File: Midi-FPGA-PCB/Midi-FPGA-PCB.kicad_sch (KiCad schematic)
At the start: 20 parts, among them Q1 DMP2123L, SW1 Boot, SW2 Reset, U1 ESP32-WROOM-32, U2 AP7361EA

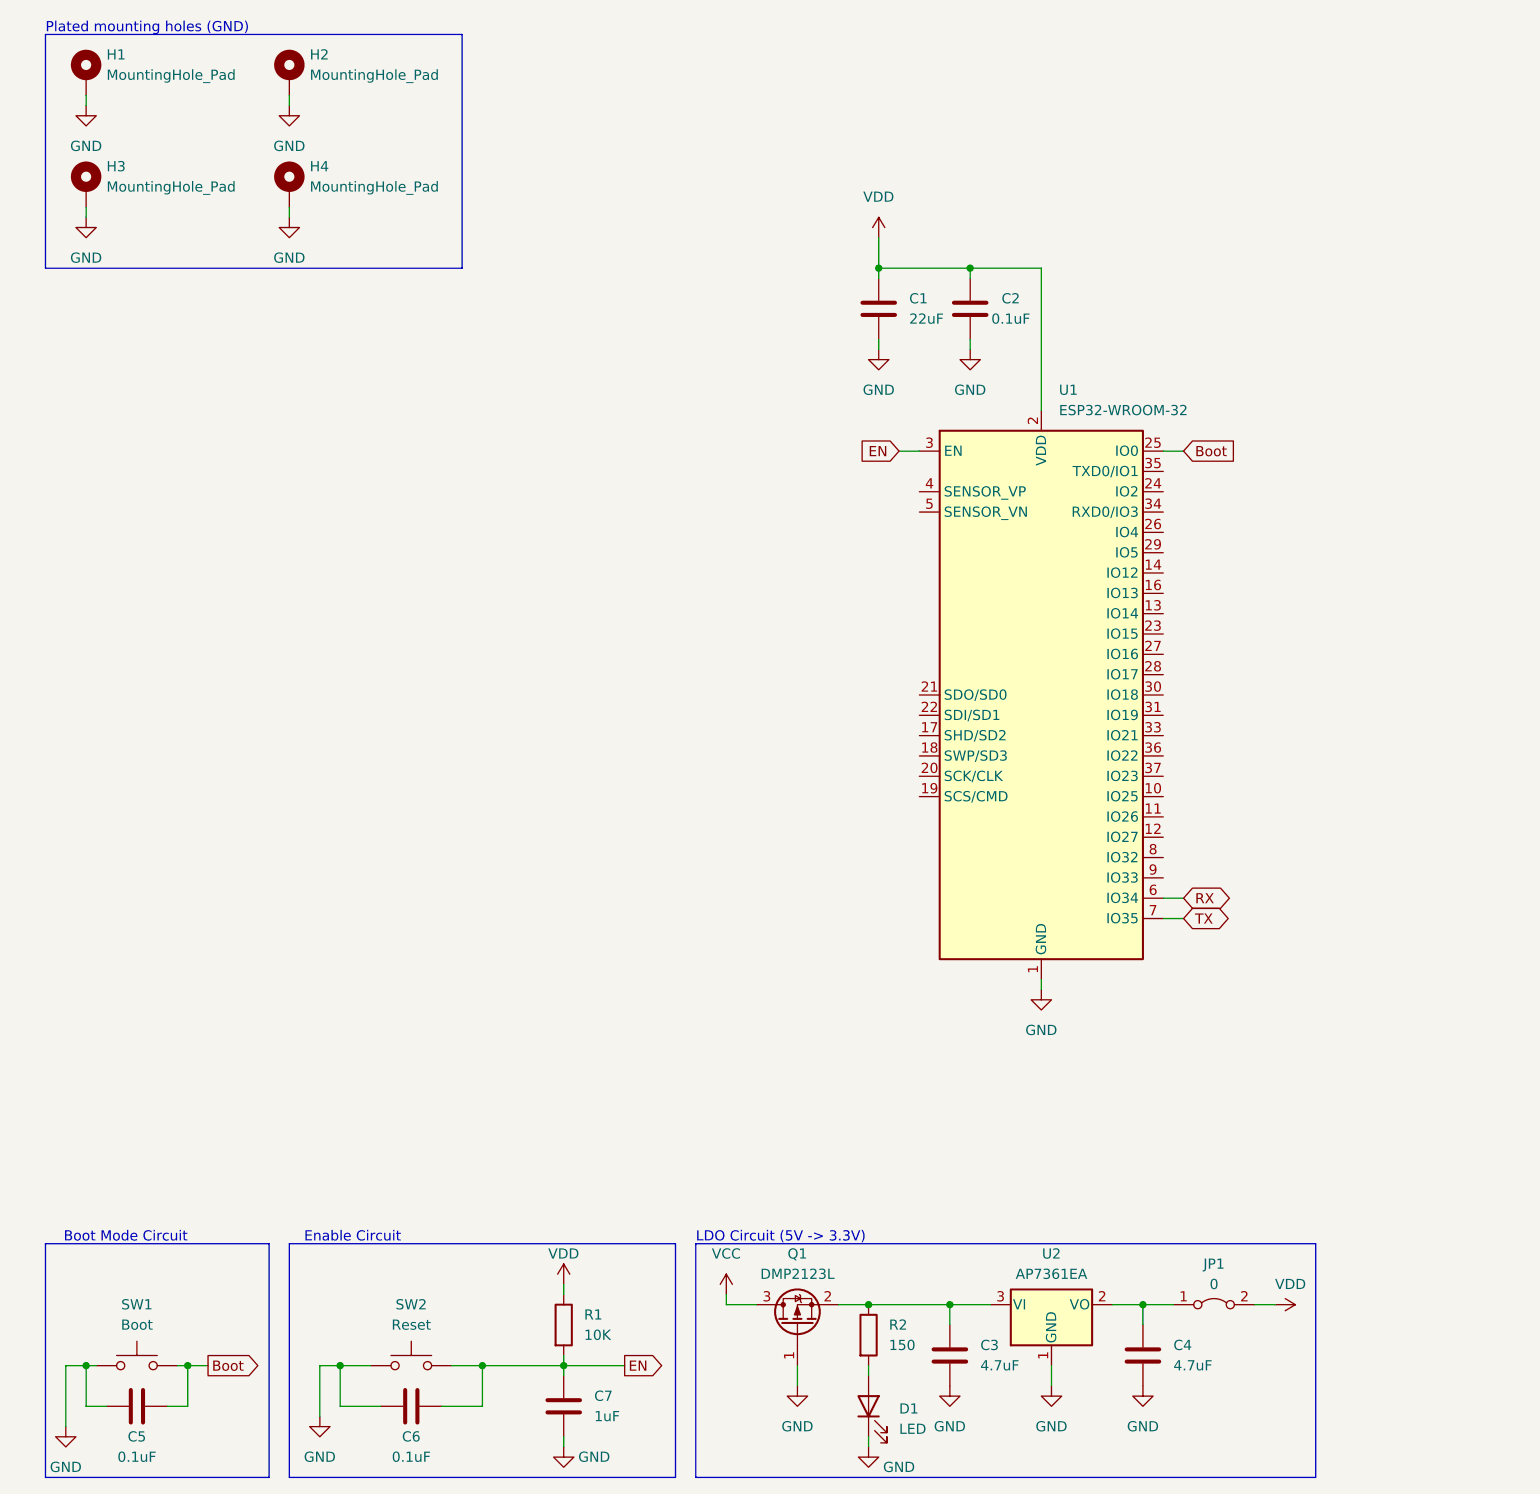
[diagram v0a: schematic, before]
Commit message: Added USB circuit
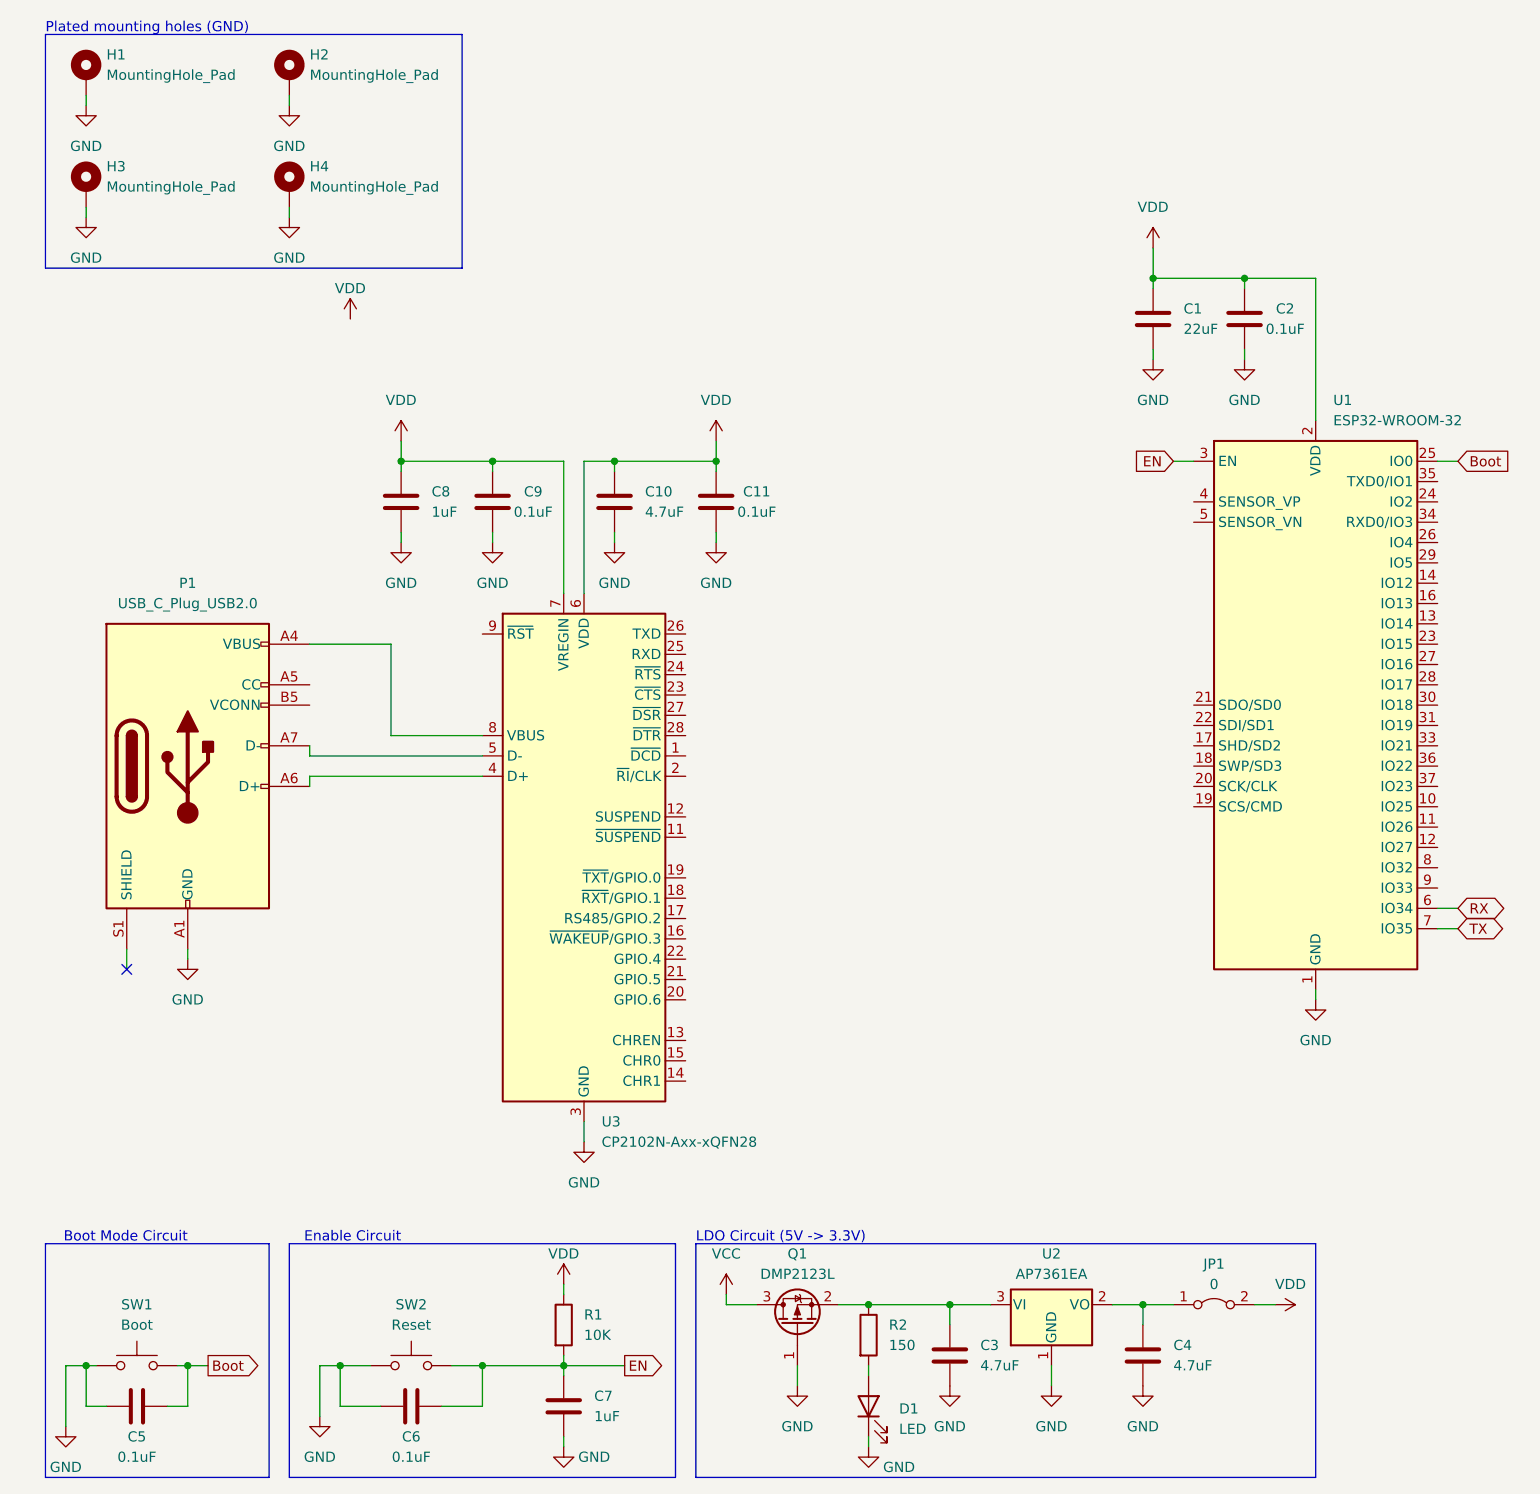
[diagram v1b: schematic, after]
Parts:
- removed U1: ESP32-WROOM-32, Midi-FPGA-lib:ESP32-WROOM-32 (No Thermal), symbol Midi-FGPA-lib:ESP32-WROOM-32_(No_Thermal)
- added C10: 4.7uF, Capacitor_SMD:C_0805_2012Metric_Pad1.18x1.45mm_HandSolder, symbol Device:C
- added C11, C9: 0.1uF, Capacitor_SMD:C_0805_2012Metric_Pad1.18x1.45mm_HandSolder, symbol Device:C
- added C8: 1uF, Capacitor_SMD:C_0805_2012Metric_Pad1.18x1.45mm_HandSolder, symbol Device:C
- added P1: USB_C_Plug_USB2.0, symbol Connector:USB_C_Plug_USB2.0
- added U1: ESP32-WROOM-32, Midi-FPGA-lib:ESP32-WROOM-32, symbol RF_Module:ESP32-WROOM-32
- added U3: CP2102N-Axx-xQFN28, Package_DFN_QFN:QFN-28-1EP_5x5mm_P0.5mm_EP3.35x3.35mm, symbol Interface_USB:CP2102N-Axx-xQFN28
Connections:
- net Boot: now also U1.25 (IO0)
- net EN: now also U1.3 (EN)
- net GND: now also C10.2, C11.1, C8.2, C9.1, P1.A1 (GND), P1.A12 (GND), P1.B1 (GND), P1.B12 (GND), U1.1 (GND), U1.15 (GND), U1.38 (GND), U1.39 (GND), U3.29 (GND), U3.3 (GND)
- net RX: now also U1.6 (IO34)
- net TX: now also U1.7 (IO35)
- net VDD: now also C10.1, C11.2, C8.1, C9.2, U1.2 (VDD), U3.6 (VDD), U3.7 (VREGIN)
- new net: P1.A4 (VBUS), P1.A9 (VBUS), P1.B4 (VBUS), P1.B9 (VBUS), U3.8 (VBUS)
- new net: P1.A6 (D+), U3.4 (D+)
- new net: P1.A7 (D-), U3.5 (D-)
- no-connect marks 0 -> 1
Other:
- moved on the sheet: C1, C2

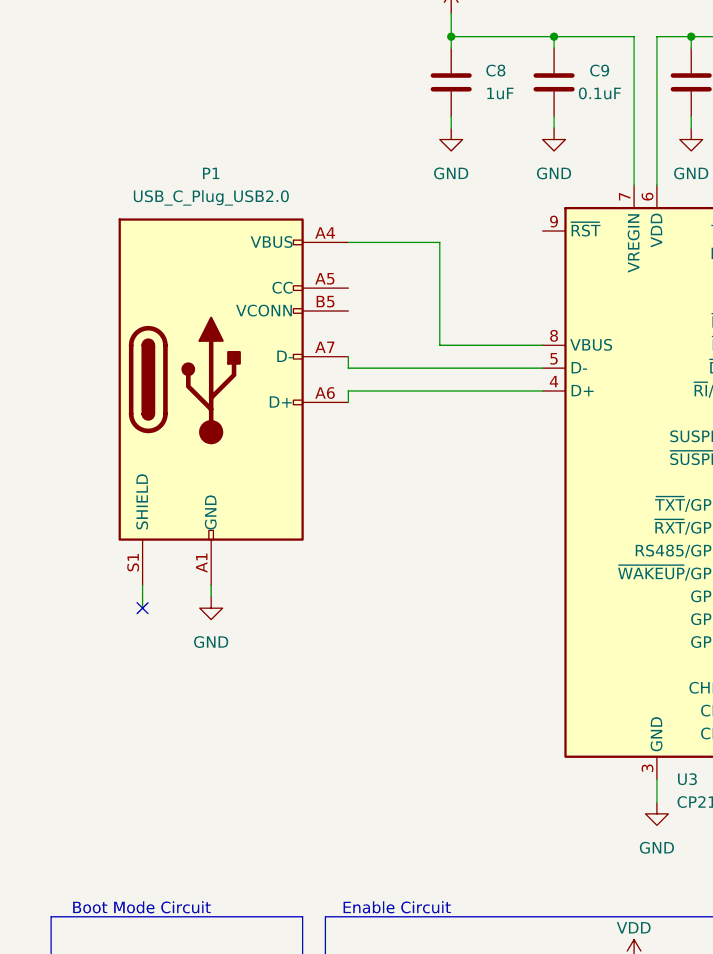
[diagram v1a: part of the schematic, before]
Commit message: Added custom usb c library
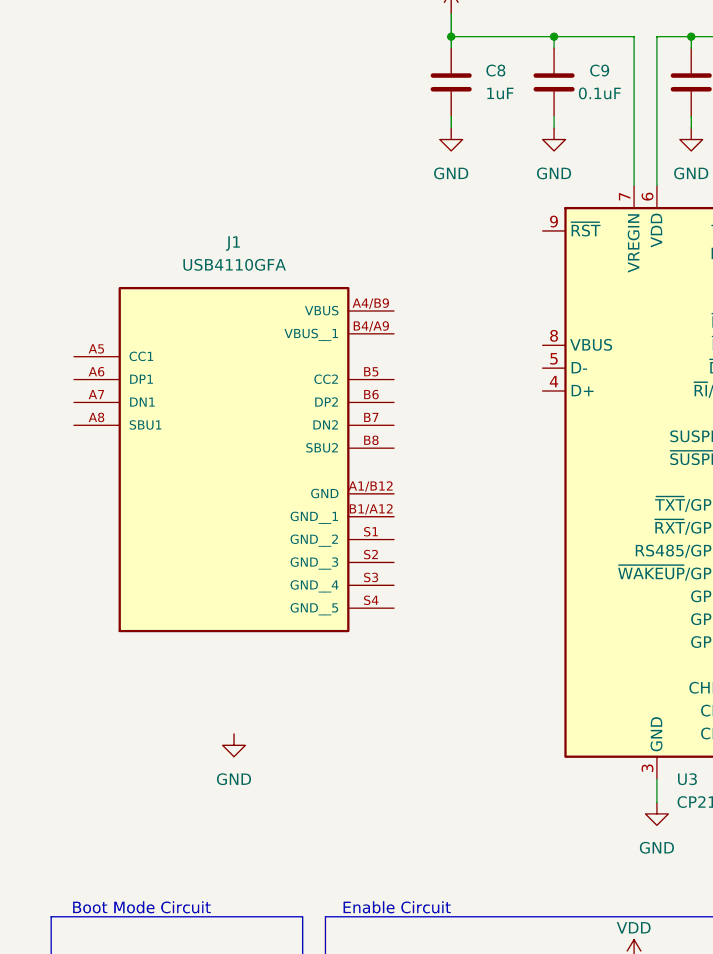
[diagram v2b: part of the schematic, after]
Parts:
- removed P1: USB_C_Plug_USB2.0, symbol Connector:USB_C_Plug_USB2.0
- added J1: USB4110GFA, USB4110_GF_A:GCT_USB4110GFA, symbol USB4110GFA:USB4110GFA
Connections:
- no-connect marks 1 -> 0
